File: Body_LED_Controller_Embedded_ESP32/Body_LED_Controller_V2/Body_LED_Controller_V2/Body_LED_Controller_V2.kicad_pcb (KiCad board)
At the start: 4 copper layers, 114 x 73 mm, 102 parts, among them J1 SERIAL, J10 USB_B_Micro, J11 USB_B_Micro, J12 UnSW_BATT_IN, J13 Conn_02x03_Odd_Even, J14 DomeControllerUSB, J15 DomePlateControllerUSB, J16 UnSW_BATT_PASS, J17 RADH_POW, J18 RASP_POW, J19 5V_OUT_3, J2 I2C, J20 ICSP, J21 DomeElectronicsPowerIn, J22 DB25_Female_MountingHoles, J23 Amplifier_POW, J3 Conn_02x10_Odd_Even, J4 LDP/MAINT, J5 COIN/VU, J6 Batt Level LEDS, J7 Data Panel/ CBI, J8 Spectrum Analyzer, J9 Ext Mic, SW1 SW_Push, SW2 SW_Push, U1 ATMEGA256016AU, U14 D36V50F5-STEPDOWN, U2 CH340C, U3 CJ2301_S1, U4 ESP32-WROOM-32U_16MB_, U5 CH340C, U6 UMH3N, U7 ME6211C33M5G, U8 CJ2301_S1, Y1 16MHz

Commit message: Added a lot since last check in
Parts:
- removed D1, D2: SMD-LED-CLEAR-BLUE(0402), Custom:LED-0402
- removed the G*** at (210.0, 69.6)
- removed the G*** at (210.0, 32.9)
- removed the G*** at (210.3, 51.3)
- removed R15, R16: 1K, Resistor_SMD:R_0402_1005Metric
- removed R4, R5: 10K, Resistor_SMD:R_0402_1005Metric
- added G***: LOGO, Logos:R2_Logo_V2, F.Cu at (170.3, 89.4)
- added G***: LOGO, Logos:Dome_Icon, F.Cu at (83.1, 51.4)
- added G***: LOGO, Logos:BodyControllerV2, F.Cu at (151.3, 88.8)
- added G***: LOGO, Logos:R2_Logo_V2, F.Cu at (132.3, 89.4)
- added J24: Future, Connector_Molex:Molex_KK-254_AE-6410-03A_1x03_P2.54mm_Vertical, F.Cu at (164.8, 113.6)
- added J25: Stealth, Connector_Molex:Molex_KK-254_AE-6410-03A_1x03_P2.54mm_Vertical, F.Cu at (147.3, 113.6)
- added J26: RADH, Connector_Molex:Molex_KK-254_AE-6410-03A_1x03_P2.54mm_Vertical, F.Cu at (156.1, 113.6)
- added J27: VU Data Panel, Connector_Molex:Molex_KK-254_AE-6410-06A_1x06_P2.54mm_Vertical, F.Cu at (173.2, 60.2)
- J1: value SERIAL -> Body Servos; footprint Connector_PinHeader_2.54mm:PinHeader_2x04_P2.54mm_Vertical -> Connector_Molex:Molex_KK-254_AE-6410-03A_1x03_P2.54mm_Vertical
- J13: value Conn_02x03_Odd_Even -> Batt Level LEDS; footprint Connector_PinHeader_2.54mm:PinHeader_2x03_P2.54mm_Vertical -> Connector_Molex:Molex_KK-254_AE-6410-04A_1x04_P2.54mm_Vertical
- J2: value I2C -> Body Servos; footprint Connector_PinHeader_2.54mm:PinHeader_2x04_P2.54mm_Vertical -> Connector_Molex:Molex_KK-254_AE-6410-03A_1x03_P2.54mm_Vertical
- J4: value LDP/MAINT -> LDP; footprint Connector_PinHeader_2.54mm:PinHeader_2x04_P2.54mm_Vertical -> Connector_Molex:Molex_KK-254_AE-6410-04A_1x04_P2.54mm_Vertical
- J5: value COIN/VU -> Coin Slots; footprint Connector_PinHeader_2.54mm:PinHeader_2x06_P2.54mm_Vertical -> Connector_Molex:Molex_KK-254_AE-6410-06A_1x06_P2.54mm_Vertical
- J6: footprint Connector_PinHeader_2.54mm:PinHeader_1x04_P2.54mm_Vertical -> Connector_Molex:Molex_KK-254_AE-6410-04A_1x04_P2.54mm_Vertical
- J7: footprint Connector_PinHeader_2.54mm:PinHeader_1x05_P2.54mm_Vertical -> Connector_Molex:Molex_KK-254_AE-6410-05A_1x05_P2.54mm_Vertical
- J8: footprint Connector_PinHeader_2.54mm:PinHeader_1x06_P2.54mm_Vertical -> Connector_Molex:Molex_KK-254_AE-6410-06A_1x06_P2.54mm_Vertical
- J9: value Ext Mic -> Maintenance; footprint Connector_PinHeader_2.54mm:PinHeader_1x03_P2.54mm_Vertical -> Connector_Molex:Molex_KK-254_AE-6410-04A_1x04_P2.54mm_Vertical
- moved R11 131.7 mm to (170.5, 58.0), turned to 90 degrees
- moved R19 116.5 mm to (136.3, 64.3)
- moved R9 107.4 mm to (170.5, 52.4), turned to 90 degrees
- moved C4 104.4 mm to (94.0, 77.2)
- moved R10 104.2 mm to (170.5, 60.9), turned to -90 degrees
- moved C3 103.8 mm to (95.4, 74.0), turned to 180 degrees
- moved C5 102.1 mm to (99.0, 83.8), turned to 180 degrees
- moved R3 100.6 mm to (107.3, 76.8)
- moved C6 98.7 mm to (100.3, 73.5)
- moved R21 97.7 mm to (89.8, 109.3), turned to -90 degrees
- moved CR2 96.9 mm to (85.5, 110.1), turned to 180 degrees
- moved C13 95.5 mm to (84.3, 107.7), turned to -90 degrees
- moved R8 95.2 mm to (170.5, 50.0), turned to -90 degrees
- moved R33 94.4 mm to (161.7, 96.5), turned to 90 degrees
- moved REF** 92.7 mm to (152.3, 71.3)
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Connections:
- J1 pad 1: +5V -> GND
- J1 pad 3: GND -> EXT_MIC
- J13 pad 2: GND -> +5V
- J13 pad 4: RX_ST -> TX_MP
- J2 pad 1: +5V -> GND
- J2 pad 2: +5V -> RX_BS
- J2 pad 3: GND -> TX_BS
- J4 pad 2: GND -> +5V
- J4 pad 3: +5V -> LDP_CLOCK
- J4 pad 4: +5V -> Net-(J4-Pad4)
- J5 pad 2: GND -> +5V
- J5 pad 3: +5V -> CS1_CLOCK
- J5 pad 4: +5V -> Net-(J5-Pad4)
- J5 pad 5: CS1_CLOCK -> CS2_CLOCK
- J5 pad 6: VU1_CLOCK -> Net-(J5-Pad6)
- J9 pad 3: EXT_MIC -> MAINT_CLOCK
- L2 pad 4: +3.3V_BC -> +5V
- R10 pad 2: Net-(J5-Pad8) -> Net-(J27-Pad4)
- R11 pad 2: Net-(J5-Pad12) -> Net-(J27-Pad6)
- R6 pad 1: Net-(J4-Pad7) -> Net-(J4-Pad4)
- R7 pad 2: Net-(J4-Pad8) -> Net-(J9-Pad4)
- R8 pad 1: Net-(J5-Pad7) -> Net-(J5-Pad4)
- R9 pad 1: Net-(J5-Pad11) -> Net-(J5-Pad6)
- U1 pad 43: SCL -> unconnected-(U1-Pad43)
- U1 pad 44: SDA -> unconnected-(U1-Pad44)
- U1 pad 45: RX1 -> unconnected-(U1-Pad45)
- U1 pad 46: TX1 -> unconnected-(U1-Pad46)
- U1 pad 63: RX3 -> unconnected-(U1-Pad63)
- U1 pad 64: TX3 -> unconnected-(U1-Pad64)
- U4 pad 10: TX_BL -> RX_FU
- U4 pad 11: RX_BL -> TX_FU
- U4 pad 13: TX_ST -> TX_BS
- U4 pad 14: RX_ST -> unconnected-(U4-Pad14)
- U4 pad 16: unconnected-(U4-Pad16) -> RX_BS
- U4 pad 23: TX_BS -> RX_BL
- U4 pad 27: RX_BS -> TX_BL
- U4 pad 28: RX_MP -> TX_RD
- U4 pad 29: TX_MP -> ST_LED_D_BC
- U4 pad 30: ST_LED_D_BC -> TX_MP
- U4 pad 31: unconnected-(U4-Pad31) -> TX_ST
- U4 pad 34: unconnected-(U4-Pad34) -> RXD0_BC
- U4 pad 6: unconnected-(U4-Pad6) -> RX_RD
- U4 pad 7: unconnected-(U4-Pad7) -> RX_ST
- U4 pad 8: unconnected-(U4-Pad8) -> RX_MP
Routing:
- net +5V: track 0.00 -> 290.0 mm, vias 0 -> 2
- net GND: track 0.00 -> 237.6 mm, vias 0 -> 28
- net +5V_BL: track 0.00 -> 154.4 mm, vias 0 -> 3
- net SPECTRUM_RIGHT: track 0.00 -> 123.5 mm, vias 0 -> 1
- net VU2_CLOCK: track 0.00 -> 123.2 mm, vias 0 -> 1
- net EXT_MIC: track 0.00 -> 122.8 mm, vias 0 -> 1
- net RESET_BL: track 0.00 -> 120.8 mm, vias 0 -> 5
- net VU2_DATA: track 0.00 -> 120.5 mm, vias 0 -> 2
- net SPECTRUM_LEFT: track 0.00 -> 115.4 mm, vias 0 -> 1
- net TX_RD: track 0.00 -> 110.7 mm, vias 0 -> 1
- net CS1_CLOCK: track 0.00 -> 107.8 mm, vias 0 -> 1
- net YELLOW_LED: track 0.00 -> 106.4 mm, vias 0 -> 2
- net D+_BL: track 0.00 -> 106.3 mm, vias 0 -> 2
- net D-_BL: track 0.00 -> 100.2 mm, vias 0 -> 2
- net DP_DATA_IN: track 0.00 -> 97.6 mm, vias 0 -> 2
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- added copper zone on F.Cu, net +12V
- added copper zone on F.Cu, net +5V
- added copper zone on B.Cu, net GND
- added copper zone on In1.Cu, net GND
- added copper zone on F.Cu, net SW_BATT_IN_POS
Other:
- board size 114 x 73 mm -> 123 x 78 mm
- board text added: "Battery Status LEDs"
- board text added: "Body Controller"
- board text added: "Body LED Controller"
- board text added: "Body Servos"
- board text added: "Coin Slots"
- board text added: "Dome Controller"
- board text added: "Dome Plate Controller"
- board text added: "Dome Power"
- board text added: "Future Serial"
- board text added: "ICSP"
- board text added: "LDP LEDs"
- board text added: "Lft"
- board text added: "Limit"
- board text added: "MP3 Trigger"
- board text added: "Maintenance LEDs"
- board text added: "Mi"
- board text added: "Mo"
- board text added: "RADH"
- board text added: "Rgt"
- board text added: "Rst"
- board text added: "Spectrum Analyzer"
- board text added: "Str"
- board text added: "Uregulated Voltage"
- board text added: "V"
- board text removed: "3V"
- board text removed: "A"
- board text removed: "BC"
- board text removed: "BL"
- board text removed: "BS"
- board text removed: "Batt LEDs"
- board text removed: "Coin"
- board text removed: "ESP-WROOM-32D"
- board text removed: "Future"
- board text removed: "I2C (2560)"
- board text removed: "ICSP (MEGA)"
- board text removed: "LDP"
- board text removed: "LED Controller"
- board text removed: "Limit Switches"
- board text removed: "MP3 T"
- board text removed: "Maint"
- board text removed: "Master Controller"
- board text removed: "Power In 12-24V"
- board text removed: "Power Out (5V)"
- board text removed: "Reset"
- board text removed: "SPEC ANY"
- board text removed: "Ser1"
- board text removed: "Ser3"
- board text removed: "Serial (ESP)"
- board text removed: "Serial (Mega)"
- board text removed: "Servo Controller"
- board text removed: "Servo Expander"

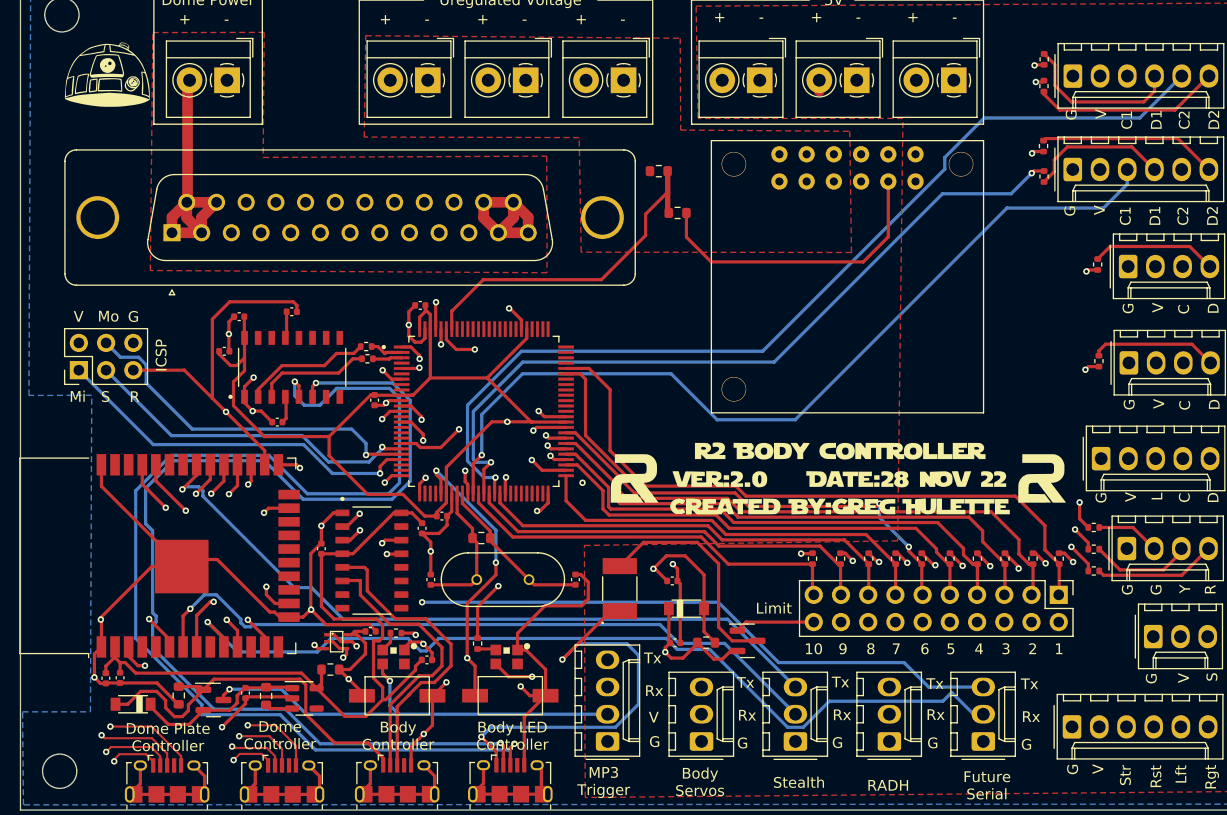
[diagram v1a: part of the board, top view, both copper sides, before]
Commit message: added LED PCBs
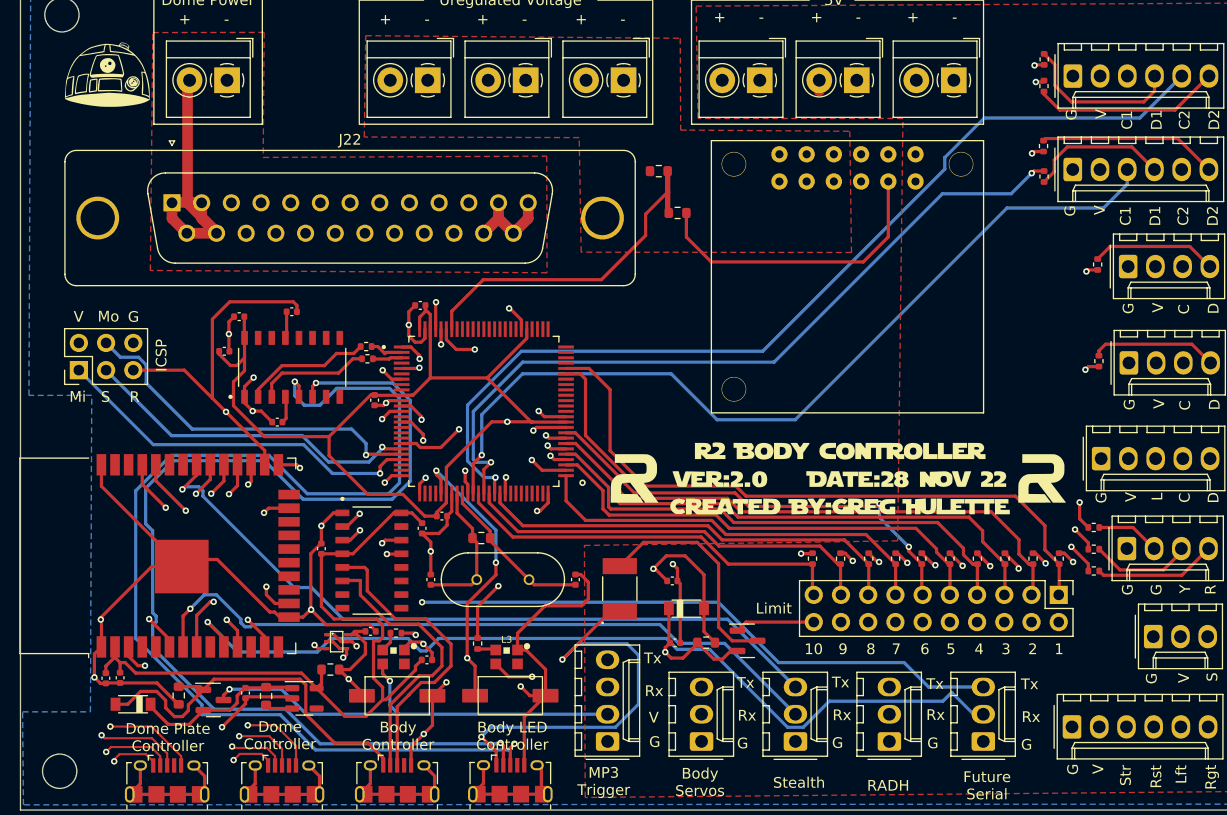
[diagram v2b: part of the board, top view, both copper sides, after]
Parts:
- J22: footprint Connector_Dsub:DSUB-25_Female_Vertical_P2.77x2.84mm_MountingHoles -> Connector_Dsub:DSUB-25_Male_Vertical_P2.77x2.84mm_MountingHoles
- U4: value ESP32-WROOM-32U_16MB_ -> ESP32-WROOM-32D_16MB_
- moved J22 2.79 mm to (89.1, 63.3), turned to 0 degrees
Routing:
- net SW_BATT_IN_POS: track 43.0 -> 36.6 mm
- net GND_DP: track 79.9 -> 84.2 mm
- net D-_DC: track 84.0 -> 80.2 mm
- net D+_DC: track 70.6 -> 66.9 mm
- net VBUS_DP: track 72.5 -> 69.3 mm
- net D+_DP: track 72.6 -> 75.7 mm
- net GND_DC: track 66.9 -> 64.0 mm
- net VBUS_DC: track 65.5 -> 68.3 mm
- net D-_DP: track 72.6 -> 70.9 mm
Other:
- board text added: "Manufactured by JLCPCB"
- board text added: "Order #: JLCJLCJLCJLC"
